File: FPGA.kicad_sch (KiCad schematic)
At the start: 46 parts, among them SW1 SW_Push

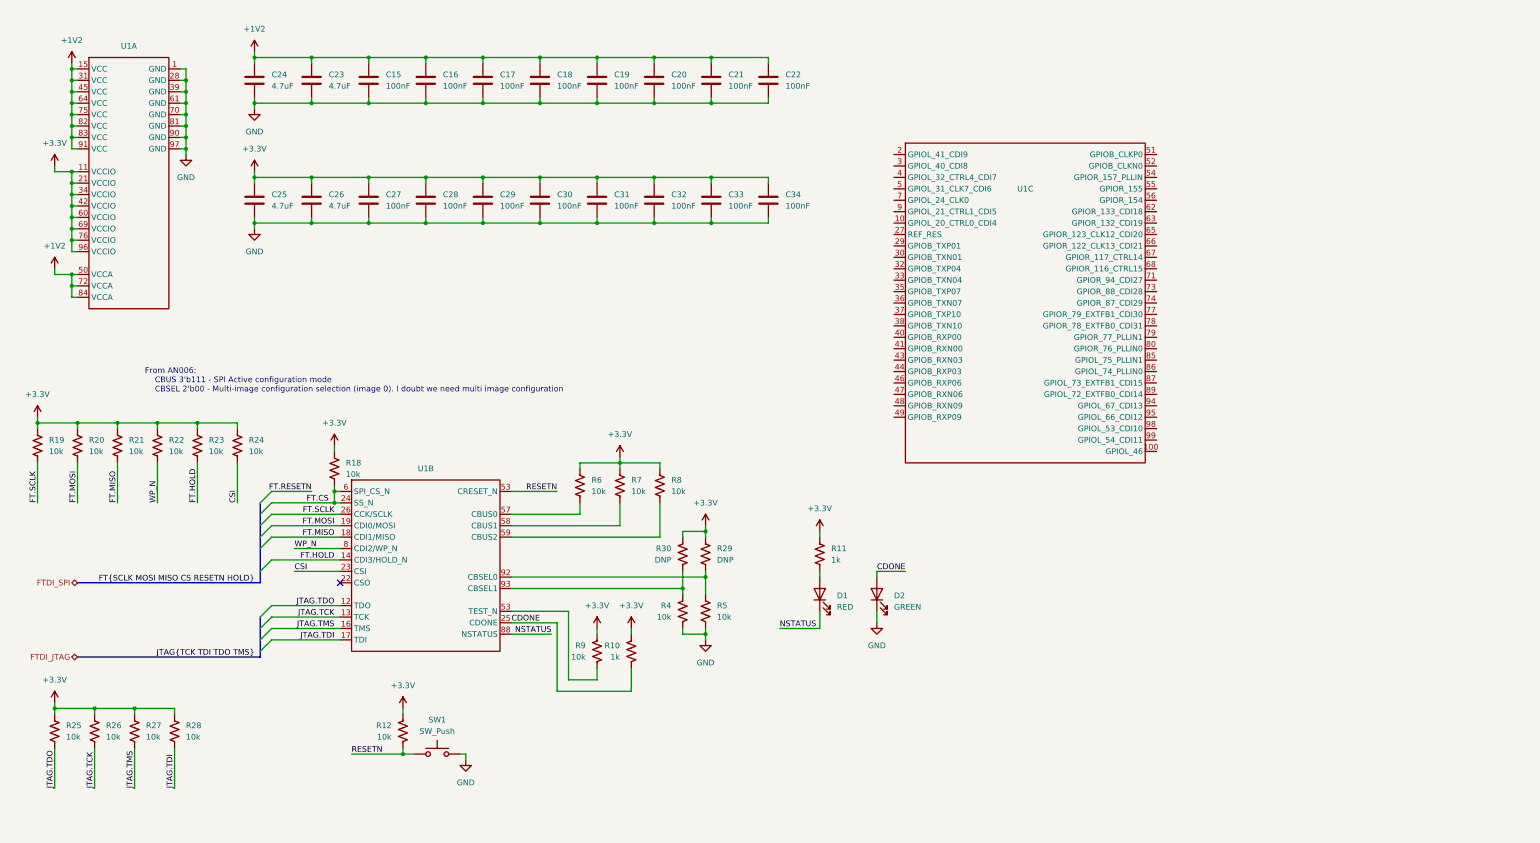
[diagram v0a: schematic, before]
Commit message: Added SRAM and removed old ADC
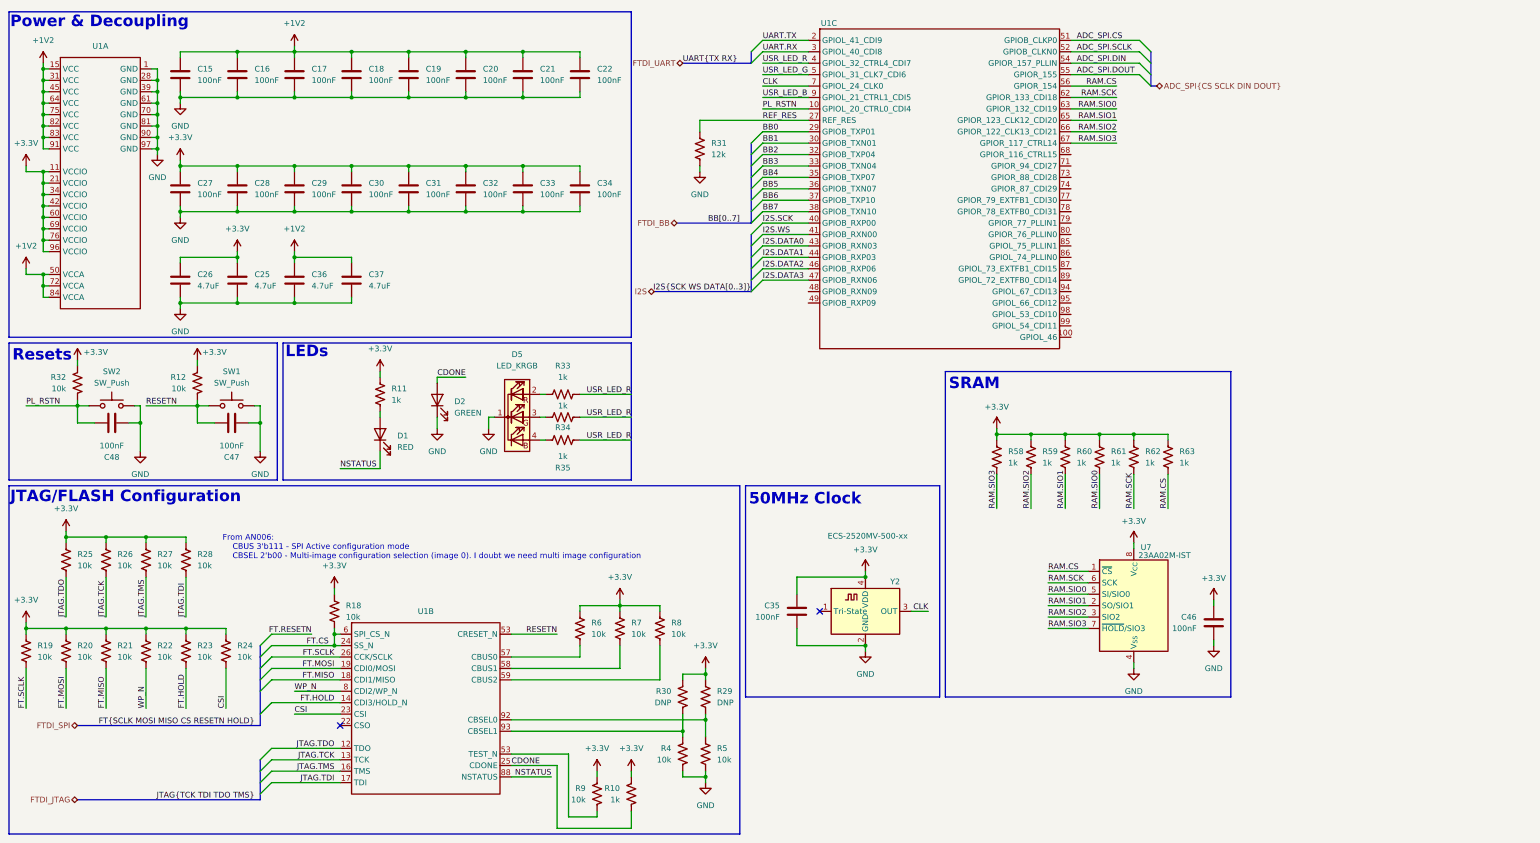
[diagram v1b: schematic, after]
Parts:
- removed C23, C24: 4.7uF, Capacitor_SMD:C_0603_1608Metric, symbol Device:C
- added C35, C46, C47, C48: 100nF, Capacitor_SMD:C_0603_1608Metric, symbol Device:C
- added C36, C37: 4.7uF, Capacitor_SMD:C_0603_1608Metric, symbol Device:C
- added D5: LED_KRGB, symbol Device:LED_KRGB
- added R31: 12k, Resistor_SMD:R_0603_1608Metric, symbol Device:R_US
- added R32: 10k, Resistor_SMD:R_0603_1608Metric, symbol Device:R_US
- added R33, R34, R35, R58, R59, R60, R61, R62, R63: 1k, Resistor_SMD:R_0603_1608Metric, symbol Device:R_US
- added SW2: SW_Push, symbol Switch:SW_Push
- added U7: 23AA02M-IST, Package_SO:TSSOP-8_4.4x3mm_P0.65mm, symbol Memory_RAM:23AA02M-IST
- added Y2: ECS-2520MV-500-xx, Oscillator:Oscillator_SMD_ECS_2520MV-xxx-xx-4Pin_2.5x2.0mm, symbol Oscillator:ECS-2520MV-xxx-xx
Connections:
- net +1V2: now also C36.1, C37.1
- net +3.3V: now also C35.1, C46.1, R32.1, R58.1, R59.1, R60.1, R61.1, R62.1, R63.1, U7.8 (V_{CC}), Y2.4 (VDD)
- net GND: now also C35.2, C36.2, C37.2, C46.2, C47.1, C48.1, D5.1 (K), R31.2, SW2.2, U7.4 (V_{SS}), Y2.2 (GND)
- net RESETN: now also C47.2
- net PL_RSTN: now reaches U1.10 (GPIOL_20_CTRL0_CDI4)
- net PL_RSTN: now also C48.2, R32.2, SW2.1
- net UART.TX: now reaches U1.2 (GPIOL_41_CDI9)
- net REF_RES: now reaches U1.27 (REF_RES)
- net REF_RES: now also R31.1
- net BB0: now reaches U1.29 (GPIOB_TXP01)
- net UART.RX: now reaches U1.3 (GPIOL_40_CDI8)
- net BB1: now reaches U1.30 (GPIOB_TXN01)
- net BB2: now reaches U1.32 (GPIOB_TXP04)
- net BB3: now reaches U1.33 (GPIOB_TXN04)
- net BB4: now reaches U1.35 (GPIOB_TXP07)
- net BB5: now reaches U1.36 (GPIOB_TXN07)
- net BB6: now reaches U1.37 (GPIOB_TXP10)
- net BB7: now reaches U1.38 (GPIOB_TXN10)
- net USR_LED_R: now reaches U1.4 (GPIOL_32_CTRL4_CDI7)
- net USR_LED_R: now also R33.2, R34.2, R35.1
- net I2S.SCK: now reaches U1.40 (GPIOB_RXP00)
- net I2S.WS: now reaches U1.41 (GPIOB_RXN00)
- net I2S.DATA0: now reaches U1.43 (GPIOB_RXN03)
- net I2S.DATA1: now reaches U1.44 (GPIOB_RXP03)
- net I2S.DATA2: now reaches U1.46 (GPIOB_RXP06)
- net I2S.DATA3: now reaches U1.47 (GPIOB_RXN06)
- net USR_LED_G: now reaches U1.5 (GPIOL_31_CLK7_CDI6)
- net ADC_SPI.CS: now reaches U1.51 (GPIOB_CLKP0)
- net ADC_SPI.SCLK: now reaches U1.52 (GPIOB_CLKN0)
- net ADC_SPI.DIN: now reaches U1.54 (GPIOR_157_PLLIN)
- net ADC_SPI.DOUT: now reaches U1.55 (GPIOR_155)
- net RAM.CS: now reaches U1.56 (GPIOR_154)
- net RAM.CS: now also R63.2, U7.1 (~{CS})
- net RAM.SCK: now reaches U1.62 (GPIOR_133_CDI18)
- net RAM.SCK: now also R62.2, U7.6 (SCK)
- net RAM.SIO0: now reaches U1.63 (GPIOR_132_CDI19)
- net RAM.SIO0: now also R61.2, U7.5 (SI/SIO0)
- net RAM.SIO1: now reaches U1.65 (GPIOR_123_CLK12_CDI20)
- net RAM.SIO1: now also R60.2, U7.2 (SO/SIO1)
- net RAM.SIO2: now reaches U1.66 (GPIOR_122_CLK13_CDI21)
- net RAM.SIO2: now also R59.2, U7.3 (SIO2)
- net RAM.SIO3: now reaches U1.67 (GPIOR_117_CTRL14)
- net RAM.SIO3: now also R58.2, U7.7 (~{HOLD}/SIO3)
- net CLK: now reaches U1.7 (GPIOL_24_CLK0)
- net CLK: now also Y2.3 (OUT)
- net USR_LED_B: now reaches U1.9 (GPIOL_21_CTRL1_CDI5)
- new net: D5.4 (BA), R35.2
- new net: D5.2 (RA), R33.1
- new net: D5.3 (GA), R34.1
- no-connect marks 1 -> 2
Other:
- note added: "50MHz Clock"
- note added: "JTAG/FLASH Configuration"
- note added: "LEDs"
- note added: "Power & Decoupling"
- note added: "Resets"
- note added: "SRAM"
- moved on the sheet: C15, C16, C17, C18, C19, C20, C21, C22, C27, C28, C29, C30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

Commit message: Initial design
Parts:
- added TP25, TP26, TP27, TP28, TP29, TP30, TP31, TP32, TP33: TestPoint, TestPoint:TestPoint_Pad_D2.0mm, symbol Connector:TestPoint
- C15, C16, C17, C18, C19, C20, C21, C22, C27, C28, C29, C30, C31, C32, C33, C34, C35, C46, C47, C48: Digikey PN (none) -> 1276-6854-1-ND; Unit Cost (none) -> 0.055
- C25, C26, C36, C37: Digikey PN (none) -> 1276-1044-1-ND; Unit Cost (none) -> 0.044
- D1: Digikey PN (none) -> 754-1123-1-ND; Unit Cost (none) -> 0.21
- D2: Digikey PN (none) -> 754-1121-1-ND; Unit Cost (none) -> 0.19
- D5: footprint (none) -> LED_SMD:LED_LiteOn_LTST-C19HE1WT; Digikey PN (none) -> 160-2162-1-ND; Unit Cost (none) -> 0.44
- R10, R11, R33, R34, R35, R58, R59, R60, R61, R62, R63: Digikey PN (none) -> 311-1.00KHRCT-ND; Unit Cost (none) -> 0.025
- R12, R18, R19, R20, R21, R22, R23, R24, R25, R26, R27, R28, R32, R4, R5, R6, R7, R8, R9: Digikey PN (none) -> 311-10KLDCT-ND; Unit Cost (none) -> 0.028
- R29, R30: now not fitted; now left out of the parts list
- R31: Digikey PN (none) -> 311-12.0KHRCT-ND; Unit Cost (none) -> 0.10
- SW1, SW2: footprint (none) -> Button_Switch_SMD:SW_Push_1P1T_NO_CK_KMR2; Digikey PN (none) -> CKN10244CT-ND; Unit Cost (none) -> 0.67
- U1: DigiKey PN (none) -> 2134-T20Q100F3C3-ND; Digikey PN (none) -> 2134-T20Q100F3C3-ND; Link https://www.digikey.com/en/products/detail/efinix-inc/T13Q1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 -> https://www.digikey.com/en/products/detail/efinix-inc/T20Q1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; Unit Cost (none) -> 10.30
- U7: Digikey PN (none) -> 150-23AA02M-I/ST-ND; Unit Cost (none) -> 3.18
- Y2: Digikey PN (none) -> XC2758CT-ND; Unit Cost (none) -> 1.20
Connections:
- net CDONE: now also TP25.1
- net CLK: now also TP33.1
- net FT.RESETN: now also C47.2, R12.2, SW1.1, U1.20 (CRESET_N)
- net NSTATUS: now also TP26.1
- net RAM.CS: now also TP27.1
- net RAM.SCK: now also TP28.1
- net RAM.SIO0: now also TP29.1
- net RAM.SIO1: now also TP30.1
- net RAM.SIO2: now also TP31.1
- net RAM.SIO3: now also TP32.1
- net USR_LED_B: now also R35.1
- net USR_LED_G: now also R34.2
- net USR_LED_R: no longer R34.2, R35.1
- removed net RESETN: C47.2, R12.2, SW1.1, U1.53 (TEST_N)
- no-connect marks 2 -> 21
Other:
- moved on the sheet: C35, Y2

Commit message: Added ethernet
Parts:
- added JP2: SolderJumper_2_Bridged, Jumper:SolderJumper-2_P1.3mm_Bridged_RoundedPad1.0x1.5mm, symbol Jumper:SolderJumper_2_Bridged
- TP25, TP26, TP27, TP28, TP29, TP30, TP31, TP32, TP33: now left out of the parts list
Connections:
- net ADC_SPI.CS: now also U1.63 (GPIOR_132_CDI19); no longer U1.51 (GPIOB_CLKP0)
- net ADC_SPI.DIN: now also U1.66 (GPIOR_122_CLK13_CDI21); no longer U1.54 (GPIOR_157_PLLIN)
- net ADC_SPI.DOUT: now also U1.67 (GPIOR_117_CTRL14); no longer U1.55 (GPIOR_155)
- net ADC_SPI.SCLK: now also U1.65 (GPIOR_123_CLK12_CDI20); no longer U1.52 (GPIOB_CLKN0)
- net CLK: now also JP2.1 (A)
- net RAM.CS: now also U1.68 (GPIOR_116_CTRL15); no longer U1.56 (GPIOR_154)
- net RAM.SCK: now also U1.71 (GPIOR_94_CDI27); no longer U1.62 (GPIOR_133_CDI18)
- net RAM.SIO0: now also U1.73 (GPIOR_88_CDI28); no longer U1.63 (GPIOR_132_CDI19)
- net RAM.SIO1: now also U1.74 (GPIOR_87_CDI29); no longer U1.65 (GPIOR_123_CLK12_CDI20)
- net RAM.SIO2: now also U1.77 (GPIOR_79_EXTFB1_CDI30); no longer U1.66 (GPIOR_122_CLK13_CDI21)
- net RAM.SIO3: now also U1.78 (GPIOR_78_EXTFB0_CDI31); no longer U1.67 (GPIOR_117_CTRL14)
- net RMII.INT: now reaches U1.100 (GPIOL_46)
- net GPIO0: now reaches U1.48 (GPIOB_RXN09)
- net GPIO1: now reaches U1.49 (GPIOB_RXP09)
- net RMII.TXD0: now reaches U1.79 (GPIOR_77_PLLIN1)
- net RMII.TXD1: now reaches U1.80 (GPIOR_76_PLLIN0)
- net RMII.TXEN: now reaches U1.85 (GPIOL_75_PLLIN1)
- net RMII.RXD0: now reaches U1.86 (GPIOL_74_PLLIN0)
- net RMII.RXD1: now reaches U1.87 (GPIOL_73_EXTFB1_CDI15)
- net RMII.RXER: now reaches U1.89 (GPIOL_72_EXTFB0_CDI14)
- net RMII.CRS_DV: now reaches U1.94 (GPIOL_67_CDI13)
- net RMII.MDIO: now reaches U1.95 (GPIOL_66_CDI12)
- net RMII.MDC: now reaches U1.98 (GPIOL_53_CDI10)
- net RMII.RSTN: now reaches U1.99 (GPIOL_54_CDI11)
- new net GPIO2: U1.51 (GPIOB_CLKP0)
- new net GPIO3: U1.52 (GPIOB_CLKN0)
- new net GPIO4: U1.54 (GPIOR_157_PLLIN)
- new net GPIO5: U1.55 (GPIOR_155)
- new net GPIO6: U1.56 (GPIOR_154)
- new net GPIO7: U1.62 (GPIOR_133_CDI18)
- new net RMII.CLK: JP2.2 (B)
- no-connect marks 21 -> 2

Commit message: Cleanup
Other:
- title: (none) -> FPGA
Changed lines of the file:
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@@
 	(generator_version "10.0")
 	(paper "A4")
+	(title_block
+		(title "FPGA")
+		(date "2026-09-19")
+	)
 	(rectangle
 		(start 73.66 86.36)
@@
 		)
 	)
-	(bus
-		(pts
-			(xy 266.7 44.45) (xy 267.97 44.45)
-		)
-		(stroke
-			(width 0)
-			(type default)
-		)
-	)
 	(wire
 		(pts
@@
 		)
 	)
+	(bus
+		(pts
+			(xy 281.94 48.26) (xy 281.94 45.72)
+		)
+		(stroke
+			(width 0)
+			(type default)
+		)
+	)
 	(wire
 		(pts
@@
 	(bus
 		(pts
+			(xy 281.94 45.72) (xy 266.7 45.72)
+		)
+		(stroke
+			(width 0)
+			(type default)
+		)
+	)
+	(bus
+		(pts
 			(xy 68.58 153.67) (xy 68.58 156.21)
 		)
@@
 	(bus
 		(pts
-			(xy 266.7 36.83) (xy 266.7 44.45)
+			(xy 266.7 36.83) (xy 266.7 45.72)
 		)
 		(stroke
@@
 	(bus
 		(pts
-			(xy 267.97 90.17) (xy 266.7 90.17)
+			(xy 265.43 90.17) (xy 266.7 90.17)
 		)
 		(stroke
@@
 	(hierarchical_label "ADC_SPI{CS SCLK DIN DOUT}"
 		(shape bidirectional)
-		(at 267.97 44.45 0)
+		(at 281.94 48.26 270)
 		(effects
 			(font
 				(size 1.27 1.27)
 			)
-			(justify left)
+			(justify right)
 		)
 	)
 	(hierarchical_label "RMII{TXD[0..1] TXEN RXD[0..1] RXER CRS_DV MDIO MDC RSTN INT CLK}"
 		(shape bidirectional)
-		(at 267.97 90.17 0)
+		(at 265.43 90.17 180)
 		(effects
 			(font
 				(size 1.27 1.27)
 			)
-			(justify left)
+			(justify right)
 		)
 	)

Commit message: Annotated schematic
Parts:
- renumbered C48 to C1, C29 to C10, C36 to C11, C18 to C12, C30 to C13, C37 to C14, C19 to C15, C31 to C16, C20 to C17, C32 to C18, C21 to C19, C15 to C2, C33 to C20, C22 to C21, C34 to C22, C35 to C23, C46 to C24, C27 to C3, C26 to C4, C47 to C5, C16 to C6, C28 to C7, C25 to C8, C17 to C9, D5 to D3, JP2 to JP1, R19 to R1, R23 to R10, R12 to R11, R24 to R12, R18 to R13, R11 to R14, R33 to R15, R34 to R16, R35 to R17, R6 to R18, R9 to R19, R25 to R2, R7 to R20, R10 to R21, R8 to R22, R30 to R23, R4 to R24, R31 to R25, R29 to R26, R5 to R27, R58 to R28, R59 to R29, R20 to R3, R60 to R30, R61 to R31, R62 to R32, R63 to R33, R32 to R4, R26 to R5, R21 to R6, R27 to R7, R22 to R8, R28 to R9, SW2 to SW1, SW1 to SW2, TP26 to TP1, TP25 to TP2, TP33 to TP3, TP27 to TP4, TP28 to TP5, TP29 to TP6, TP30 to TP7, TP31 to TP8, TP32 to TP9, U7 to U2, Y2 to Y1

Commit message: Started module-level layout
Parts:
- TP1, TP2, TP3, TP4, TP5, TP6, TP7, TP8, TP9: footprint TestPoint:TestPoint_Pad_D2.0mm -> TestPoint:TestPoint_Pad_D1.0mm
- U1: footprint (none) -> Package_QFP:LQFP-100_14x14mm_P0.5mm

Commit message: More layout
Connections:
- net ADC_SPI.CS: now also U1.33 (GPIOB_TXN04); no longer U1.63 (GPIOR_132_CDI19)
- net ADC_SPI.DIN: now also U1.36 (GPIOB_TXN07); no longer U1.66 (GPIOR_122_CLK13_CDI21)
- net ADC_SPI.DOUT: now also U1.37 (GPIOB_TXP10); no longer U1.67 (GPIOR_117_CTRL14)
- net ADC_SPI.SCLK: now also U1.35 (GPIOB_TXP07); no longer U1.65 (GPIOR_123_CLK12_CDI20)
- net BB0: now also U1.62 (GPIOR_133_CDI18); no longer U1.29 (GPIOB_TXP01)
- net BB1: now also U1.63 (GPIOR_132_CDI19); no longer U1.30 (GPIOB_TXN01)
- net BB2: now also U1.65 (GPIOR_123_CLK12_CDI20); no longer U1.32 (GPIOB_TXP04)
- net BB3: now also U1.66 (GPIOR_122_CLK13_CDI21); no longer U1.33 (GPIOB_TXN04)
- net BB4: now also U1.67 (GPIOR_117_CTRL14); no longer U1.35 (GPIOB_TXP07)
- net BB5: now also U1.68 (GPIOR_116_CTRL15); no longer U1.36 (GPIOB_TXN07)
- net BB6: now also U1.71 (GPIOR_94_CDI27); no longer U1.37 (GPIOB_TXP10)
- net BB7: now also U1.73 (GPIOR_88_CDI28); no longer U1.38 (GPIOB_TXN10)
- net CLK: now also U1.86 (GPIOL_74_PLLIN0); no longer U1.7 (GPIOL_24_CLK0)
- net GPIO0: now also U1.47 (GPIOB_RXN06); no longer U1.48 (GPIOB_RXN09)
- net GPIO1: now also U1.48 (GPIOB_RXN09); no longer U1.49 (GPIOB_RXP09)
- net GPIO2: now also U1.49 (GPIOB_RXP09); no longer U1.51 (GPIOB_CLKP0)
- net GPIO3: now also U1.51 (GPIOB_CLKP0); no longer U1.52 (GPIOB_CLKN0)
- net GPIO4: now also U1.52 (GPIOB_CLKN0); no longer U1.54 (GPIOR_157_PLLIN)
- net GPIO5: now also U1.54 (GPIOR_157_PLLIN); no longer U1.55 (GPIOR_155)
- net GPIO6: now also U1.55 (GPIOR_155); no longer U1.56 (GPIOR_154)
- net GPIO7: now also U1.56 (GPIOR_154); no longer U1.62 (GPIOR_133_CDI18)
- net I2S.DATA0: now also U1.4 (GPIOL_32_CTRL4_CDI7); no longer U1.43 (GPIOB_RXN03)
- net I2S.DATA1: now also U1.5 (GPIOL_31_CLK7_CDI6); no longer U1.44 (GPIOB_RXP03)
- net I2S.DATA2: now also U1.7 (GPIOL_24_CLK0); no longer U1.46 (GPIOB_RXP06)
- net I2S.DATA3: now also U1.9 (GPIOL_21_CTRL1_CDI5); no longer U1.47 (GPIOB_RXN06)
- net I2S.SCK: now also U1.2 (GPIOL_41_CDI9); no longer U1.40 (GPIOB_RXP00)
- net I2S.WS: now also U1.3 (GPIOL_40_CDI8); no longer U1.41 (GPIOB_RXN00)
- net RAM.CS: now also U1.43 (GPIOB_RXN03); no longer U1.68 (GPIOR_116_CTRL15)
- net RAM.SCK: now also U1.40 (GPIOB_RXP00); no longer U1.71 (GPIOR_94_CDI27)
- net RAM.SIO0: now also U1.38 (GPIOB_TXN10); no longer U1.73 (GPIOR_88_CDI28)
- net RAM.SIO1: now also U1.44 (GPIOB_RXP03); no longer U1.74 (GPIOR_87_CDI29)
- net RAM.SIO2: now also U1.46 (GPIOB_RXP06); no longer U1.77 (GPIOR_79_EXTFB1_CDI30)
- net RAM.SIO3: now also U1.41 (GPIOB_RXN00); no longer U1.78 (GPIOR_78_EXTFB0_CDI31)
- net RMII.RXD0: now also U1.85 (GPIOL_75_PLLIN1); no longer U1.86 (GPIOL_74_PLLIN0)
- net RMII.TXD0: now also U1.78 (GPIOR_78_EXTFB0_CDI31); no longer U1.79 (GPIOR_77_PLLIN1)
- net RMII.TXD1: now also U1.79 (GPIOR_77_PLLIN1); no longer U1.80 (GPIOR_76_PLLIN0)
- net RMII.TXEN: now also U1.80 (GPIOR_76_PLLIN0); no longer U1.85 (GPIOL_75_PLLIN1)
- net UART.RX: now also U1.77 (GPIOR_79_EXTFB1_CDI30); no longer U1.3 (GPIOL_40_CDI8)
- net UART.TX: now also U1.74 (GPIOR_87_CDI29); no longer U1.2 (GPIOL_41_CDI9)
- net USR_LED_B: now also U1.32 (GPIOB_TXP04); no longer U1.9 (GPIOL_21_CTRL1_CDI5)
- net USR_LED_G: now also U1.30 (GPIOB_TXN01); no longer U1.5 (GPIOL_31_CLK7_CDI6)
- net USR_LED_R: now also U1.29 (GPIOB_TXP01); no longer U1.4 (GPIOL_32_CTRL4_CDI7)
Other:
- moved on the sheet: R25

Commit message: Routing done
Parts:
- removed JP1: SolderJumper_2_Bridged, Jumper:SolderJumper-2_P1.3mm_Bridged_RoundedPad1.0x1.5mm, symbol Jumper:SolderJumper_2_Bridged
- removed TP4, TP5, TP6, TP7, TP8, TP9: TestPoint, TestPoint:TestPoint_Pad_D1.0mm, symbol Connector:TestPoint
- added NT1: NetTie_2, NetTie:NetTie-2_SMD_Pad0.5mm, symbol Device:NetTie_2
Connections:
- net CLK: now also NT1.2
- net I2S.DATA0: now also U1.9 (GPIOL_21_CTRL1_CDI5); no longer U1.4 (GPIOL_32_CTRL4_CDI7)
- net I2S.DATA1: now also U1.7 (GPIOL_24_CLK0); no longer U1.5 (GPIOL_31_CLK7_CDI6)
- net I2S.DATA2: now also U1.5 (GPIOL_31_CLK7_CDI6); no longer U1.7 (GPIOL_24_CLK0)
- net I2S.DATA3: now also U1.4 (GPIOL_32_CTRL4_CDI7); no longer U1.9 (GPIOL_21_CTRL1_CDI5)
- net RMII.CLK: now also NT1.1
- net RMII.CRS_DV: now also U1.95 (GPIOL_66_CDI12); no longer U1.94 (GPIOL_67_CDI13)
- net RMII.INT: now also U1.87 (GPIOL_73_EXTFB1_CDI15); no longer U1.100 (GPIOL_46)
- net RMII.MDC: now also U1.89 (GPIOL_72_EXTFB0_CDI14); no longer U1.98 (GPIOL_53_CDI10)
- net RMII.MDIO: now also U1.94 (GPIOL_67_CDI13); no longer U1.95 (GPIOL_66_CDI12)
- net RMII.RSTN: now also U1.85 (GPIOL_75_PLLIN1); no longer U1.99 (GPIOL_54_CDI11)
- net RMII.RXD0: now also U1.99 (GPIOL_54_CDI11); no longer U1.85 (GPIOL_75_PLLIN1)
- net RMII.RXD1: now also U1.100 (GPIOL_46); no longer U1.87 (GPIOL_73_EXTFB1_CDI15)
- net RMII.RXER: now also U1.98 (GPIOL_53_CDI10); no longer U1.89 (GPIOL_72_EXTFB0_CDI14)
- net RMII.TXD0: now also U1.79 (GPIOR_77_PLLIN1); no longer U1.78 (GPIOR_78_EXTFB0_CDI31)
- net RMII.TXD1: now also U1.78 (GPIOR_78_EXTFB0_CDI31); no longer U1.79 (GPIOR_77_PLLIN1)
- net UART.RX: now also U1.74 (GPIOR_87_CDI29); no longer U1.77 (GPIOR_79_EXTFB1_CDI30)
- net UART.TX: now also U1.77 (GPIOR_79_EXTFB1_CDI30); no longer U1.74 (GPIOR_87_CDI29)
